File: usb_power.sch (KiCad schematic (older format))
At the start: 56 parts, among them J1 USB-C-16PIN, J2 M20-8770642R, J3 M20-8770642R, Q1 IRLML6402, Q2 BSS214NW, U1 FT230XS, U2 MCP1726-3302ESN, U3 MIC5319-1.8YD5-TR

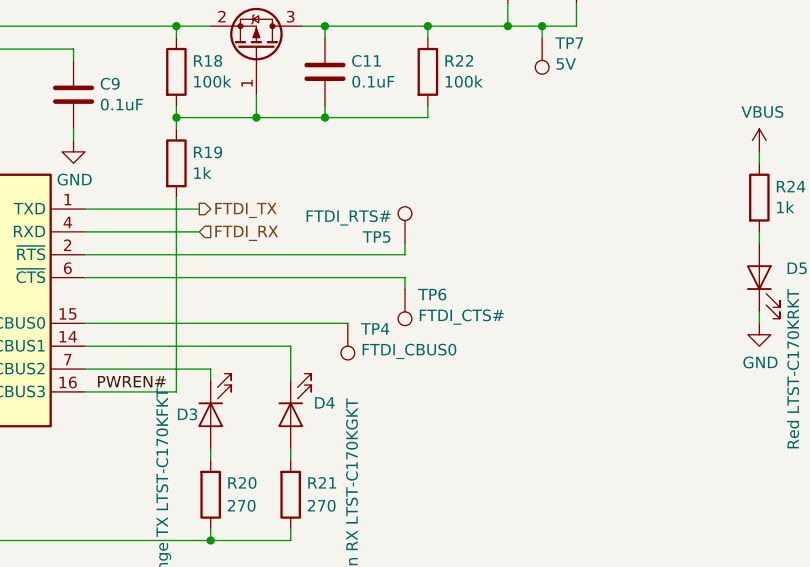
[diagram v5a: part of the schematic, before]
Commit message: Add labels for buttons
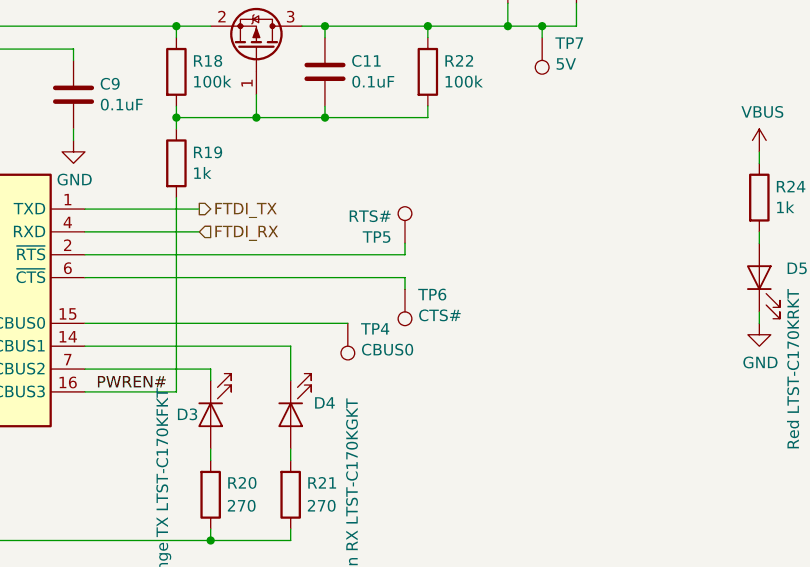
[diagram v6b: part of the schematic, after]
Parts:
- TP4: value FTDI_CBUS0 -> CBUS0
- TP5: value FTDI_RTS# -> RTS#
- TP6: value FTDI_CTS# -> CTS#
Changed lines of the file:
@@
 P 6700 2650
 F 0 "TP4" H 6642 2676 50  0000 R CNN
-F 1 "FTDI_CBUS0" H 6642 2767 50  0000 R CNN
+F 1 "CBUS0" H 6642 2767 50  0000 R CNN
 F 2 "TestPoint:TestPoint_Pad_D1.5mm" H 6900 2650 50  0001 C CNN
 F 3 "~" H 6900 2650 50  0001 C CNN
@@
 P 6950 2500
 F 0 "TP6" H 6892 2526 50  0000 R CNN
-F 1 "FTDI_CTS#" H 6892 2617 50  0000 R CNN
+F 1 "CTS#" H 6892 2617 50  0000 R CNN
 F 2 "TestPoint:TestPoint_Pad_D1.5mm" H 7150 2500 50  0001 C CNN
 F 3 "~" H 7150 2500 50  0001 C CNN
@@
 P 6950 2300
 F 0 "TP5" H 6892 2326 50  0000 R CNN
-F 1 "FTDI_RTS#" H 6892 2417 50  0000 R CNN
+F 1 "RTS#" H 6892 2417 50  0000 R CNN
 F 2 "TestPoint:TestPoint_Pad_D1.5mm" H 7150 2300 50  0001 C CNN
 F 3 "~" H 7150 2300 50  0001 C CNN
